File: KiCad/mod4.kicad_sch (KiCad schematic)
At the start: 51 parts, among them M7 Fan_4pin, M8 Fan_4pin, U4 ZD25Q64BSIGT

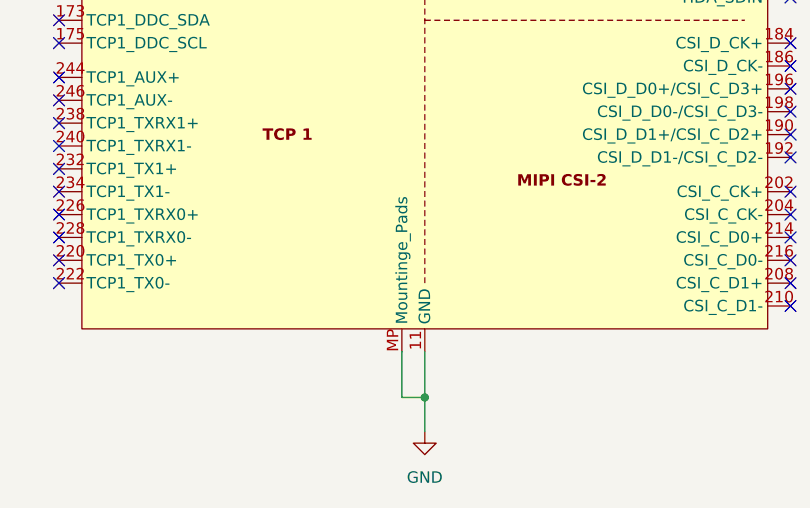
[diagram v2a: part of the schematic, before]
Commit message: Fix more footprint issues, continue laying out components
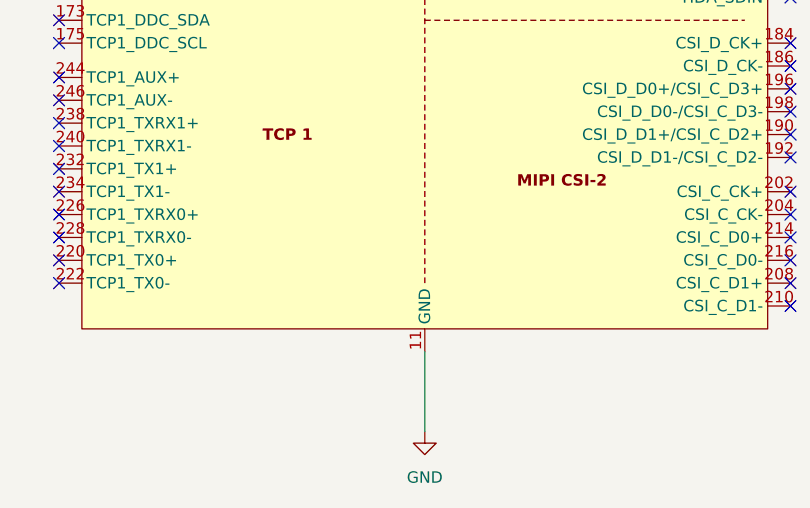
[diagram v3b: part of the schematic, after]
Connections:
- net GND: no longer A4.MP (Mountinge_Pads)
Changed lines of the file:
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@@
 	)
 	(junction
-		(at 287.02 354.33)
-		(diameter 0)
-		(color 0 0 0 0)
-	)
-	(junction
 		(at 347.98 102.87)
 		(diameter 0)
@@
 	(wire
 		(pts
-			(xy 287.02 349.25) (xy 287.02 354.33)
+			(xy 287.02 349.25) (xy 287.02 358.14)
 		)
 		(stroke
@@
 		)
 	)
-	(wire
-		(pts
-			(xy 287.02 354.33) (xy 287.02 358.14)
-		)
-		(stroke
-			(width 0)
-			(type default)
-		)
-	)
 	(bus
 		(pts
@@
 		)
 	)
-	(wire
-		(pts
-			(xy 284.48 354.33) (xy 287.02 354.33)
-		)
-		(stroke
-			(width 0)
-			(type default)
-		)
-	)
 	(bus
 		(pts
@@
 	(wire
 		(pts
-			(xy 284.48 349.25) (xy 284.48 354.33)
-		)
-		(stroke
-			(width 0)
-			(type default)
-		)
-	)
-	(wire
-		(pts
 			(xy 327.66 102.87) (xy 347.98 102.87)
 		)
@@
 		(pin "183"
 		)
-		(pin "MP"
-		)
 		(pin "137"

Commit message: Place STM32 and fix cpu fan headers
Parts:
- M7: footprint Connector:FanPinHeader_1x04_P2.54mm_Vertical -> Connector_JST:JST_PH_B4B-PH-K_1x04_P2.00mm_Vertical
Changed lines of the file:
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@@
 			)
 		)
-		(property "Footprint" "Connector:FanPinHeader_1x04_P2.54mm_Vertical"
+		(property "Footprint" "Connector_JST:JST_PH_B4B-PH-K_1x04_P2.00mm_Vertical"
 			(at 363.22 59.436 0)
 			(effects

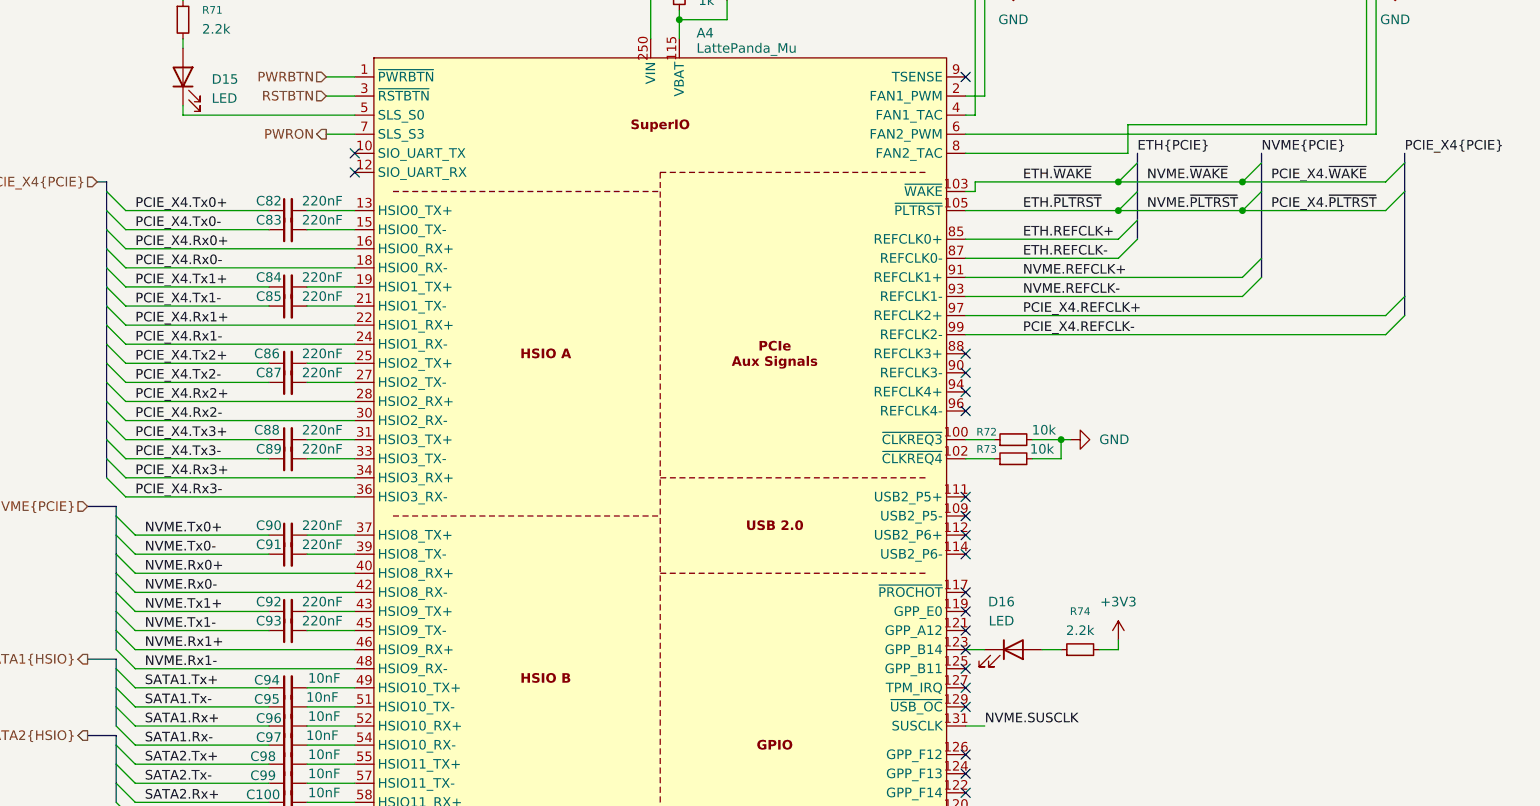
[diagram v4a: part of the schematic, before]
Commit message: Finish connecting x1 slot. Add pcie clkreq lines
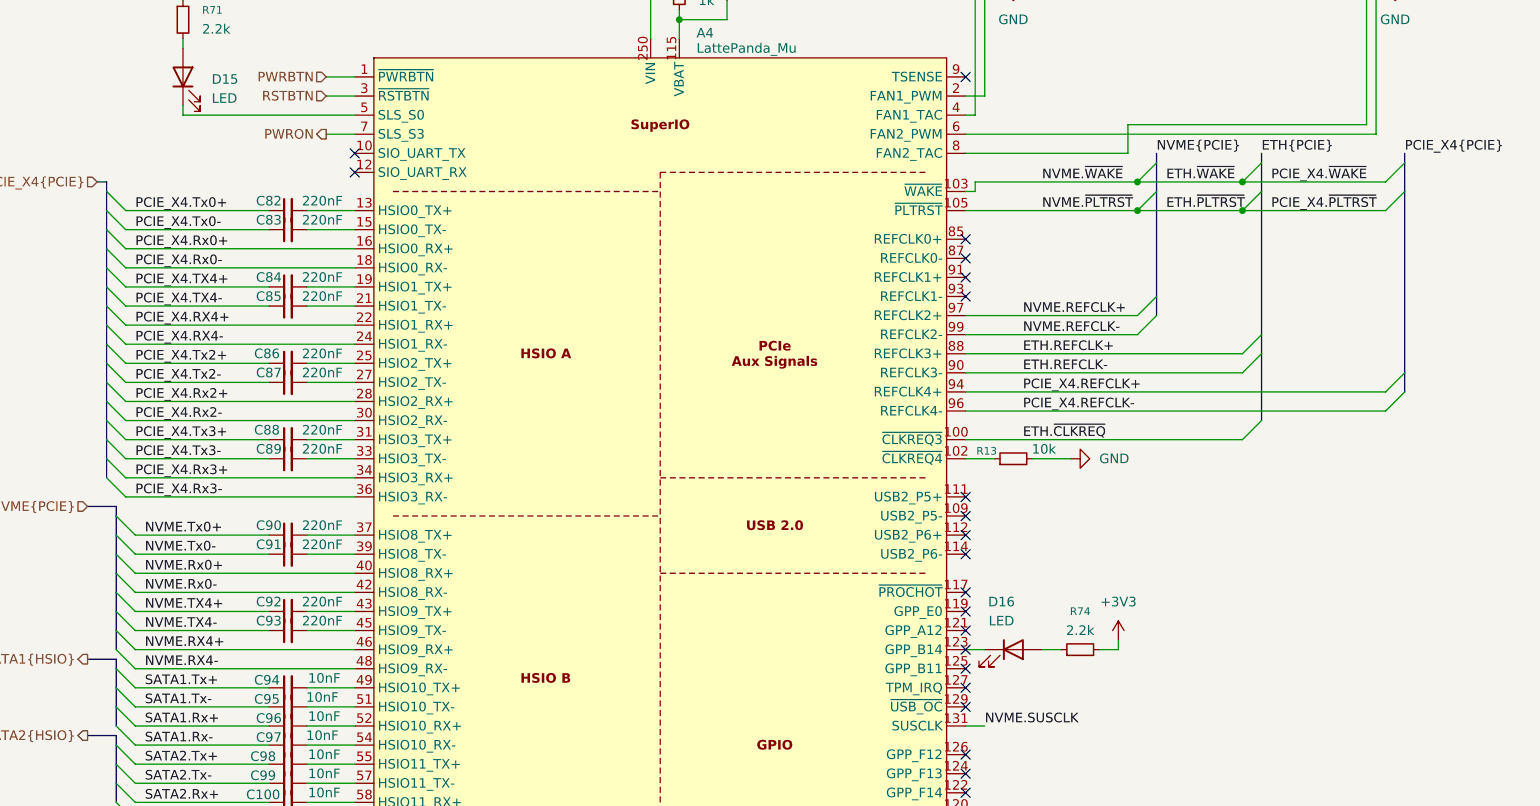
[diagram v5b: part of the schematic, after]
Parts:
- removed R72, R73: 10k, Resistor_SMD:R_0402_1005Metric, symbol Device:R_Small
- added R13: 10k, Resistor_SMD:R_0402_1005Metric, symbol Device:R_Small
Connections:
- net ETH.REFCLK+: now also A4.88 (REFCLK3+); no longer A4.85 (REFCLK0+)
- net ETH.REFCLK-: now also A4.90 (REFCLK3-); no longer A4.87 (REFCLK0-)
- net GND: now also R13.2
- net NVME.REFCLK+: now also A4.97 (REFCLK2+); no longer A4.91 (REFCLK1+)
- net NVME.REFCLK-: now also A4.99 (REFCLK2-); no longer A4.93 (REFCLK1-)
- net PCIE_X4.REFCLK+: now also A4.94 (REFCLK4+); no longer A4.97 (REFCLK2+)
- net PCIE_X4.REFCLK-: now also A4.96 (REFCLK4-); no longer A4.99 (REFCLK2-)
- net ETH.~{CLKREQ}: now reaches A4.100 (~{CLKREQ3})
- net at A4.102 (~{CLKREQ4}): now also R13.1
- net NVME.Rx1+ renamed NVME.RX4+
- net NVME.Rx1- renamed NVME.RX4-
- net NVME.Tx1+ renamed NVME.TX4+
- net NVME.Tx1- renamed NVME.TX4-
- net PCIE_X4.Rx1+ renamed PCIE_X4.RX4+
- net PCIE_X4.Rx1- renamed PCIE_X4.RX4-
- net PCIE_X4.Tx1+ renamed PCIE_X4.TX4+
- net PCIE_X4.Tx1- renamed PCIE_X4.TX4-

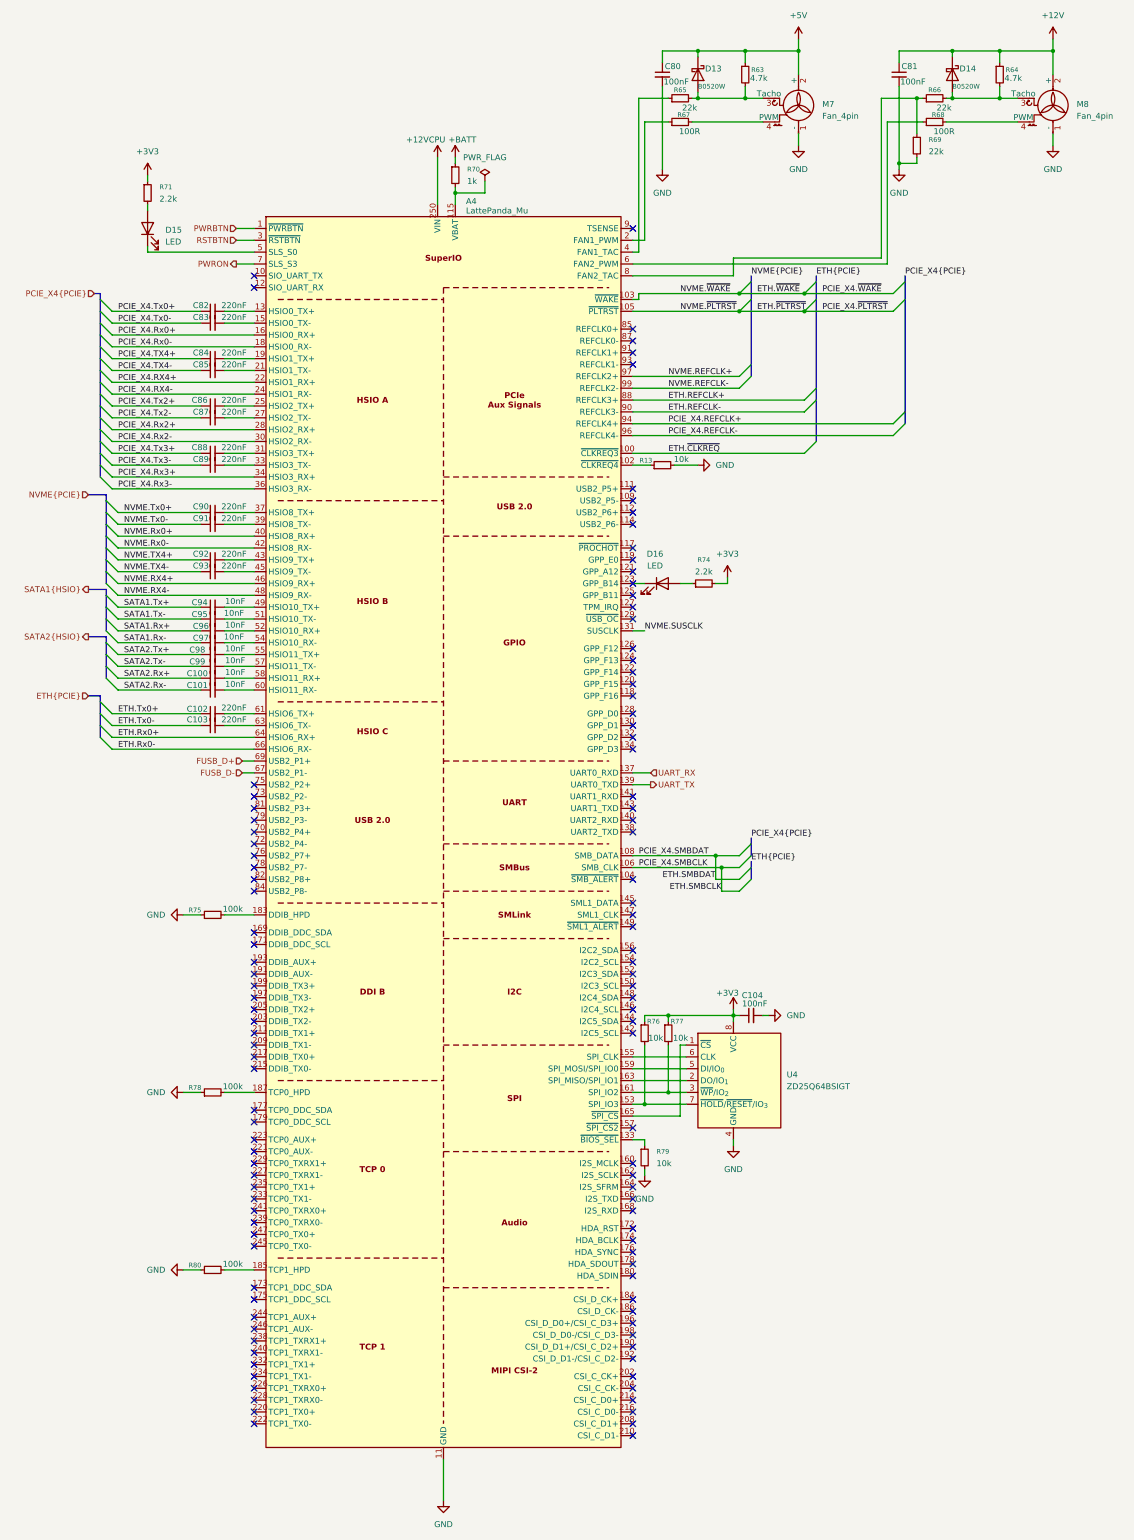
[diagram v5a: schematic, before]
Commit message: Re-annotate schematic
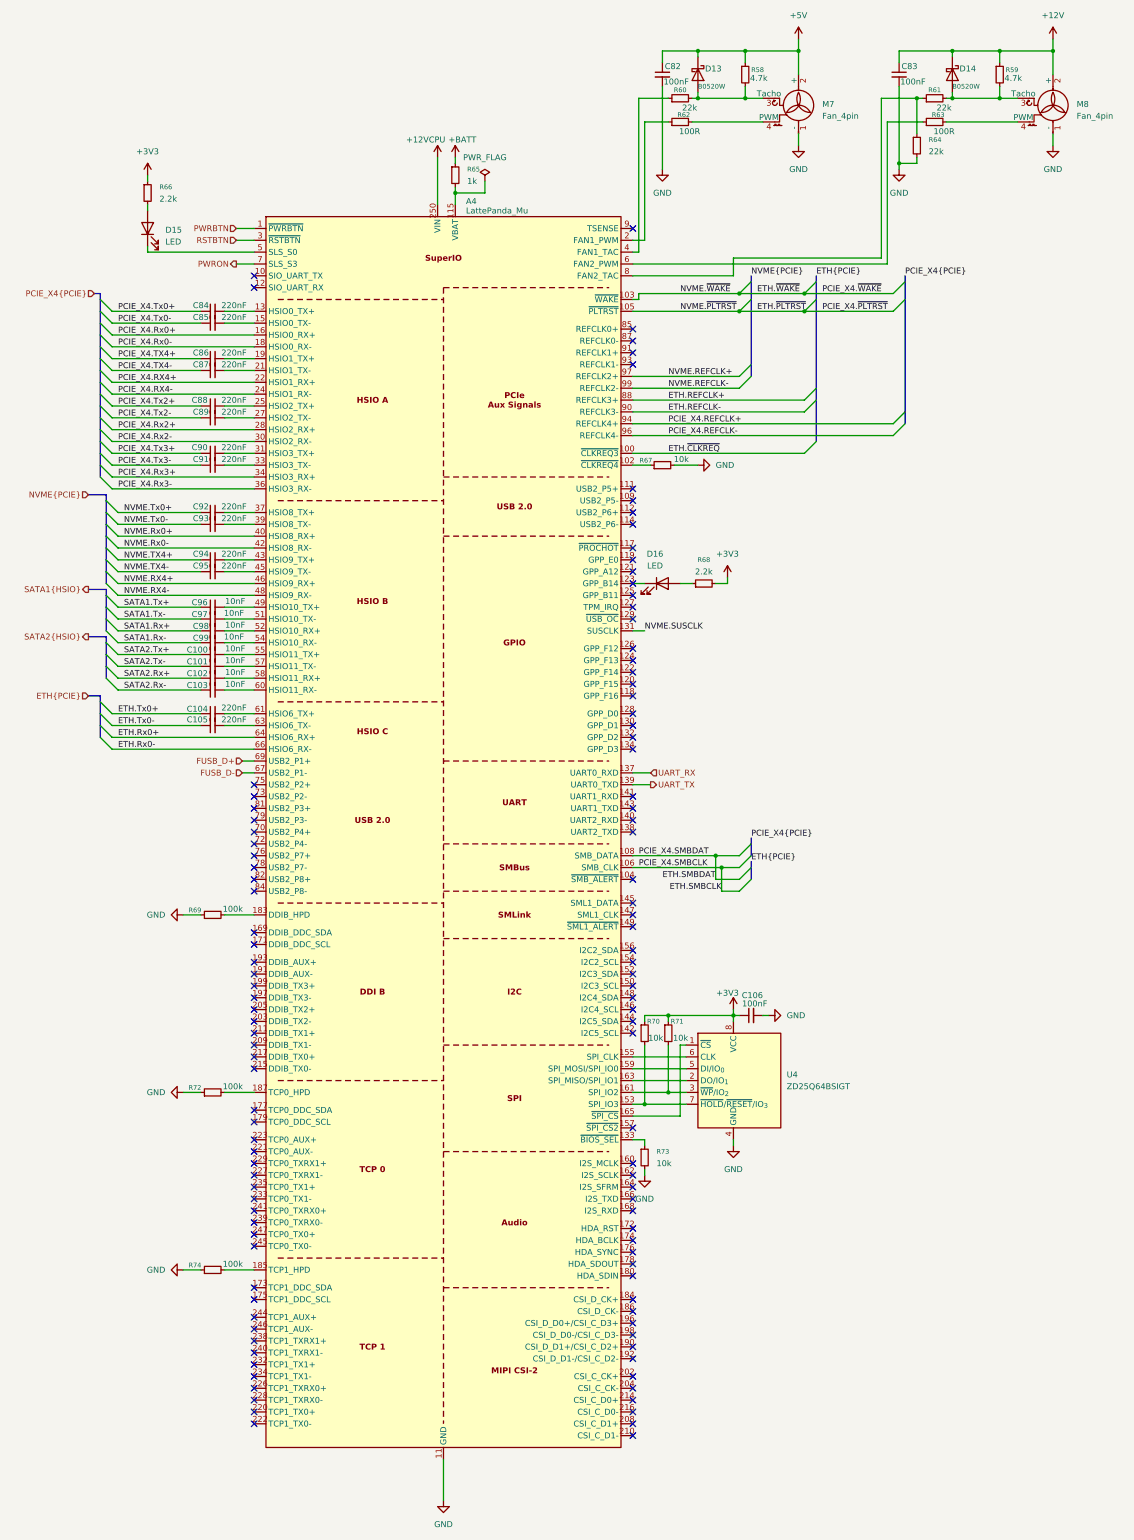
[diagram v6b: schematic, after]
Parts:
- renumbered C98 to C100, C99 to C101, C100 to C102, C101 to C103, C102 to C104, C103 to C105, C104 to C106, C80 to C82, C81 to C83, C82 to C84, C83 to C85, C84 to C86, C85 to C87, C86 to C88, C87 to C89, C88 to C90, C89 to C91, C90 to C92, C91 to C93, C92 to C94, C93 to C95, C94 to C96, C95 to C97, C96 to C98, C97 to C99, R63 to R58, R64 to R59, R65 to R60, R66 to R61, R67 to R62, R68 to R63, R69 to R64, R70 to R65, R71 to R66, R13 to R67, R74 to R68, R75 to R69, R76 to R70, R77 to R71, R78 to R72, R79 to R73, R80 to R74
